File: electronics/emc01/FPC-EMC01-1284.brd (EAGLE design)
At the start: 100 x 86.6 mm, 59 parts, among them J1 CONN-MOLEX-MICROFIT-6PIN, J10 ICSP, J11 CONN-RECT-16PIN-2ROW, J12 CONN-RECT-16PIN-2ROW, J13 CONN-RECT-16PIN-2ROW, J14 CONN-RECT-16PIN-2ROW, J4 MOT-X, J5 MOT-Y, J6 MOT-Z, J7 CONN-RECT-3PINJST_PH_2MM, J8 CONN-RECT-3PINJST_PH_2MM, J9 CONN-RECT-3PINJST_PH_2MM, Q2 2N7002PW, Q4 16Mhz, U1 STEPSTICK, U2 STEPSTICK, U3 STEPSTICK, U4 MIC5205, U5 ATMEGA1284P-AU, U6 FT231XS

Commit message: Cleaned up EMC01 board and finalized for peer review
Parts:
- removed C18: 100uF, rcl:PANASONIC_D
- removed C19, C24: 0.1uF, SparkFun:0603-CAP
- removed C20: 10uF, SparkFun-Capacitors:EIA3216
- removed C22, C23: 47pF, SparkFun-Capacitors:0603-CAP
- removed C34, C36, C42: 100nF, dp_devices:C805
- removed J10: ICSP, FirePick:CONN-RECT-2.54MM-6-PIN-2ROW-SMTH
- removed JP5: (no value), !con-lstb:MA04-1
- removed LED4: Yellow, SparkFun-LED:LED-1206-NO_SILK
- removed Q4: 16Mhz, adafruit:CTS406
- removed R12: 1k, SparkFun:0603-RES
- removed R13, R16: 27, SparkFun-Resistors:0603-RES
- removed R17, R18: 10k, SparkFun:0603-RES
- removed U$22: USB-MINIB-5PIN, SparkFun-Connectors:USB-MINIB
- removed U4: MIC5205, SparkFun:SOT23-5
- removed U5: ATMEGA1284P-AU, Atmel_By_element14_Batch_1-00:QFP80P1200X1200X120-44N
- removed U6: FT231XS, SparkFun-DigitalIC:SSOP20_L
- added C1, C4, C5, C7, C8: 100N, SparkFun-Capacitors:0805
- added C10: 0.1uF, SparkFun-Capacitors:0805
- added C12: 47pF, SparkFun-Capacitors:0805
- added C9: 0.1, SparkFun-Capacitors:0805
- added FID1, FID2, FID3, FID4: FIDUCIAL1X2, SparkFun-Aesthetics:FIDUCIAL-1X2
- added J15: (no value), !con-lstb:MA04-1
- added J16: ICSP, FirePick:CONN-RECT-2.54MM-6-PIN-2ROW-SMTH
- added J2: CONN-MOLEX-MICROFIT-6PIN, FirePick:CONN-MOLEX-MINIFIT-6PIN-2ROW
- added J4A: MOT-X, FirePick:CONN-JST-PH_2.0MM_4PIN-SMT-RA
- added J5A: MOT-Y, FirePick:CONN-JST-PH_2.0MM_4PIN-SMT-RA
- added J6A: MOT-Z, FirePick:CONN-JST-PH_2.0MM_4PIN-SMT-RA
- added J7A, J8A, J9A: (no value), FirePick:CONN-JST_PH-2.0MM-3PIN-SMT-RA
- added LED2: Red, SparkFun-LED:LED-1206-NO_SILK
- added LOGO1: FIREPICK-LOGO, FirePick:FIREPICK-LOGO
- added LOGO2: CC-BY-SA-LOGO, FirePick:CC-BY-SA-LOGO
- added LOGO3: OSHW-LOGOL, SparkFun-Aesthetics:OSHW-LOGO-L
- added R1: 10K, SparkFun-Resistors:0805
- added R6: 1k, SparkFun-Resistors:0805
- added R8: 27, SparkFun-Resistors:0805
- added STEPSTICK1, STEPSTICK2: STEPSTICK, FirePick:STEPSTICK
- added TP1: PD2, FirePick:CON-TESTPOINT
- added TP2: +12V, FirePick:CON-TESTPOINT
- added TP3: GND, FirePick:CON-TESTPOINT
- added TP4: +5V, FirePick:CON-TESTPOINT
- added TP5: +3.3V, FirePick:CON-TESTPOINT
- added U$15: CREATIVE_COMMONS, SparkFun:CREATIVE_COMMONS
- added X1: 16Mhz, adafruit:CTS406
- C11, C3: value 22pF -> 22P; device dp_devices:C805 -> SparkFun-Capacitors:0805
- C13: value 100nF -> 47pF; device dp_devices:C805 -> SparkFun-Capacitors:0805
- C14: value 100nF -> 0.1uF; device dp_devices:C805 -> SparkFun-Capacitors:0805
- C15: value 1uF -> 100uF; device SparkFun:0603-CAP -> rcl:PANASONIC_D
- C17: value 0.1uF -> 100uF; device SparkFun:0603-CAP -> rcl:PANASONIC_D
- C2: value 0.1uF -> 10uF; device ipc-7351-capacitor:CAPC2012X145AN -> rcl:PANASONIC_D
- C6: value 100uF -> 0.1uF; device rcl:PANASONIC_D -> SparkFun-Capacitors:0805
- J1: value CONN-MOLEX-MICROFIT-6PIN -> USB-MINIB-5PIN; device FirePick:CONN-MOLEX-MINIFIT-6PIN-2ROW -> SparkFun-Connectors:USB-MINIB
- J4: value MOT-X -> (none); device FirePick:CONN-JST-PH_2.0MM_4PIN-SMT-RA -> !con-lstb:MA04-1
- J5: value MOT-Y -> (none); device FirePick:CONN-JST-PH_2.0MM_4PIN-SMT-RA -> !con-lstb:MA04-1
- J6: value MOT-Z -> (none); device FirePick:CONN-JST-PH_2.0MM_4PIN-SMT-RA -> !con-lstb:MA04-1
- J7, J8, J9: value CONN-RECT-3PINJST_PH_2MM -> (none); device FirePick:CONN-JST_PH-2.0MM-3PIN-SMT-RA -> !con-lstb:MA03-1
- LED3: value Red -> Yellow
- R10, R11: value 1k -> 10k; device SparkFun:0603-RES -> SparkFun-Resistors:0805
- R2: device adafruit:R0805 -> SparkFun-Resistors:0805
- R3, R4, R5: value 10K -> 1k; device adafruit:R0805 -> SparkFun-Resistors:0805
- R7: device SparkFun:0603-RES -> SparkFun-Resistors:0805
- R9: value 1k -> 27; device SparkFun:0603-RES -> SparkFun-Resistors:0805
- U1: value STEPSTICK -> IC-ATMEGA1284P-AU; device FirePick:STEPSTICK -> FirePick:QFP44
- U2: value STEPSTICK -> FT231XS; device FirePick:STEPSTICK -> SparkFun-DigitalIC:SSOP20_L
- moved J1 73.0 mm to (50.0, 12.0), turned to 90 degrees
- moved C6 63.6 mm to (54.5, 18.6), turned to 270 degrees
- moved C15 46.4 mm to (50.3, 70.6), turned to 180 degrees
- moved C14 42.2 mm to (42.2, 19.5), turned to 90 degrees
- moved R5 40.3 mm to (65.3, 20.4)
- moved C13 39.3 mm to (52.7, 18.6), turned to 90 degrees
- moved R4 35.2 mm to (65.3, 17.5)
- moved C17 32.4 mm to (69.5, 38.9), turned to 60 degrees
- moved J3 31.7 mm to (50.0, 32.0), turned to 180 degrees
- moved Q2 31.2 mm to (59.6, 24.8), turned to 270 degrees
- moved R3 28.1 mm to (65.3, 14.6)
- moved R2 26.2 mm to (55.4, 40.2), turned to 270 degrees
- moved U2 24.2 mm to (50.0, 24.8), turned to 180 degrees
- moved S1 23.6 mm to (62.1, 10.4)
- moved R7 22.7 mm to (50.8, 29.5), turned to 0 degrees
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- renumbered U3 to STEPSTICK3
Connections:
- removed net !XYZ-ENABLE: R2.1, R3.1, R4.1, STEPSTICK3.!ENABLE!, U1.!ENABLE!, U2.!ENABLE!, U5.15
- removed net N$1: J5.4, U2.2B
- removed net N$13: J5.3, U2.2A
- removed net N$14: J5.2, U2.1A
- removed net N$15: J5.1, U2.1B
- removed net N$17: J6.4, STEPSTICK3.2B
- removed net N$18: J6.3, STEPSTICK3.2A
- removed net N$19: J6.2, STEPSTICK3.1A
- removed net N$20: J6.1, STEPSTICK3.1B
- removed net N$26: Q2.2, R17.1, U6.1
- removed net N$6: J4.4, U1.2B
- removed net N$7: J4.3, U1.2A
- removed net N$8: J4.2, U1.1A
- removed net N$9: J4.1, U1.1B
- removed net RESERVED: U5.44
- removed net X-STOP: J7.1, U5.21
- removed net Y-STOP: J8.1, U5.22
- removed net Z-STOP: J9.1, U5.23
- new net !XYZ_ENABLE: R2.1, STEPSTICK1.!ENABLE!, STEPSTICK2.!ENABLE!, STEPSTICK3.!ENABLE!, U1.15
- new net DTR_3.3V: Q2.2, R10.1, U2.1
- new net SPARE: TP1.1, U1.11
- new net X1A: J4.2, J4A.2, STEPSTICK1.1A
- new net X1B: J4.1, J4A.1, STEPSTICK1.1B
- new net X2A: J4.3, J4A.3, STEPSTICK1.2A
- new net X2B: J4.4, J4A.4, STEPSTICK1.2B
- new net X_STOP: J7.1, J7A.1, U1.24
- new net Y1A: J5.2, J5A.2, STEPSTICK2.1A
- new net Y1B: J5.1, J5A.1, STEPSTICK2.1B
- new net Y2A: J5.3, J5A.3, STEPSTICK2.2A
- new net Y2B: J5.4, J5A.4, STEPSTICK2.2B
- new net Y_STOP: J8.1, J8A.1, U1.42
- new net Z1A: J6.2, J6A.2, STEPSTICK3.1A
- new net Z1B: J6.1, J6A.1, STEPSTICK3.1B
- new net Z2A: J6.3, J6A.3, STEPSTICK3.2A
- new net Z2B: J6.4, J6A.4, STEPSTICK3.2B
- new net Z_STOP: J9.1, J9A.1, U1.12
- net !RESET: now also C9.2, J16.2, R1.1, U1.4; no longer C2.1, J10.2, R5.1, U5.4
- net +5V: now also C1.1, C2.+, C5.1, C6.1, C7.1, C8.1, J15.1, J16.5, J7A.2, J8A.2, J9A.2, R1.2, R11.2, R4.1, R5.1, STEPSTICK1.MS1, STEPSTICK1.MS2, STEPSTICK1.MS3, STEPSTICK1.VDD, STEPSTICK2.MS1, STEPSTICK2.MS2, STEPSTICK2.MS3, STEPSTICK2.VDD, TP4.1, U1.17, U1.27, U1.38, U1.5, U2.15; no longer C13.2, C14.2, C19.1, C20.A, C34.2, C36.2, J10.5, JP5.1, R10.1, R18.2, R4.2, R5.2, R7.2, R9.1, U1.MS1, U1.MS2, U1.MS3, U1.VDD, U2.MS1, U2.MS2, U2.MS3, U2.VDD, U4.1, U4.3, U5.17, U5.27, U5.38, U5.5, U6.15
- net 12V: now also C15.+, C17.+, J2.1, J2.2, J2.3, STEPSTICK1.VMOT, STEPSTICK2.VMOT, TP2.1; no longer C18.+, C6.+, J1.1, J1.2, J1.3, U1.VMOT, U2.VMOT
- net 3.3V: now also C10.1, R10.2, TP5.1, U2.13, U2.14, U2.3; no longer C15.1, C24.1, R17.2, U4.5, U6.13, U6.14, U6.3
- net AREF: now also C4.1, U1.29; no longer C42.2, U5.29
- net AVR_RXD: now also R6.1, U1.9; no longer R11.1, U5.9
- net AVR_TXD: now also R7.1, U1.10; no longer R12.1, U5.10
- net D+: now also C13.1, J1.D+, R9.1; no longer C22.1, R16.1, U$22.D+
- net D-: now also C12.1, J1.D-, R8.1; no longer C23.1, R13.1, U$22.D-
- net DTR: now also C9.1, R11.1; no longer C2.2, R18.1
- net GND: now also C1.2, C10.2, C12.2, C13.2, C14.2, C15.-, C17.-, C2.-, C4.2, C5.2, C6.2, C7.2, C8.2, J1.GND, J1.MTN1, J1.MTN2, J1.MTN3, J1.MTN4, J15.2, J16.1, J2.4, J2.5, J2.6, J7A.3, J8A.3, J9A.3, STEPSTICK1.GND, STEPSTICK1.GND@2, STEPSTICK2.GND, STEPSTICK2.GND@2, TP3.1, U1.18, U1.28, U1.39, U1.6, U2.16, U2.6; no longer C13.1, C14.1, C15.2, C17.2, C18.-, C19.2, C20.C, C22.2, C23.2, C24.2, C34.1, C36.1, C42.1, C6.-, J1.4, J1.5, J1.6, J10.1, JP5.2, U$22.GND, U$22.MTN1, U$22.MTN2, U$22.MTN3, U$22.MTN4, U1.GND, U1.GND@2, U2.GND, U2.GND@2, U4.2, U5.18, U5.28, U5.39, U5.6, U6.16, U6.6
- net MISO: now also J16.6, U1.2; no longer J10.6, U5.2
- net MOSI: now also J16.3, U1.1; no longer J10.3, U5.1
- net N$11: now also STEPSTICK1.!RESET!, STEPSTICK1.!SLEEP!; no longer U1.!RESET!, U1.!SLEEP!
- net N$16: now also STEPSTICK2.!RESET!, STEPSTICK2.!SLEEP!; no longer U2.!RESET!, U2.!SLEEP!
- net N$21: now also LED2.A, R4.2; no longer LED3.A, R9.2
- net N$22: now also LED3.A, R5.2; no longer LED4.A, R10.2
- net N$23: now also R8.2, U2.12; no longer R13.2, U6.12
- net N$25: now also R9.2, U2.11; no longer R16.2, U6.11
- net N$4: now also R3.1; no longer R7.1
- net RXD: now also R7.2, U2.4; no longer R12.2, U6.4
- net RXLED: now also LED3.C, U2.17; no longer LED4.C, U6.17
- net SCL: now also J15.3, U1.19; no longer JP5.3, U5.19
- net SCLK: now also J16.4, U1.3; no longer J10.4, U5.3
- net SDA: now also J15.4, U1.20; no longer JP5.4, U5.20
- net TOOL1_AIN: now also U1.37; no longer U5.37
- net TOOL1_DOUT: now also U1.36; no longer U5.33
- net TOOL1_ENABLE: now also U1.41; no longer U5.14
- net TOOL2_AIN: now also U1.35; no longer U5.36
- net TOOL2_DOUT: now also U1.34; no longer U5.32
- net TOOL2_ENABLE: now also U1.40; no longer U5.13
- net TOOL3_AIN: now also U1.32; no longer U5.35
- net TOOL3_DOUT: now also U1.33; no longer U5.31
- net TOOL3_ENABLE: now also U1.22; no longer U5.12
- net TOOL4_AIN: now also U1.30; no longer U5.34
- net TOOL4_DOUT: now also U1.31; no longer U5.30
- net TOOL4_ENABLE: now also U1.21; no longer U5.11
- net TOOL_DIR: now also U1.16; no longer U5.40
- net TOOL_STEP: now also U1.23; no longer U5.41
- net TXD: now also R6.2, U2.20; no longer R11.2, U6.20
- net TXLED: now also LED2.C, U2.10; no longer LED3.C, U6.10
- net VUSB: now also C14.1, J1.VBUS; no longer C17.1, U$22.VBUS
- net XTAL1: now also U1.8, X1.3; no longer Q4.3, U5.8
- net XTAL2: now also U1.7, X1.1; no longer Q4.1, U5.7
- net X_DIR: now also STEPSTICK1.DIR, U1.25; no longer U1.STEP, U5.24
- net X_STEP: now also STEPSTICK1.STEP, U1.26; no longer U1.DIR, U5.16
- net Y_DIR: now also STEPSTICK2.DIR, U1.43; no longer U2.STEP, U5.26
- net Y_STEP: now also STEPSTICK2.STEP, U1.44; no longer U2.DIR, U5.25
- net Z_DIR: now also STEPSTICK3.DIR, U1.13; no longer STEPSTICK3.STEP, U5.42
- net Z_STEP: now also STEPSTICK3.STEP, U1.14; no longer STEPSTICK3.DIR, U5.43
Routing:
- net GND: track 280.2 -> 167.5 mm, vias 8 -> 24
- net TOOL4_AIN: track 125.6 -> 29.6 mm
- net Y_DIR: track 103.5 -> 14.3 mm, vias 4 -> 1
- net !XYZ-ENABLE: track 84.2 -> 0.00 mm, vias 3 -> 0
- net TOOL2_ENABLE: track 101.5 -> 32.7 mm, vias 3 -> 2
- net !XYZ_ENABLE: track 0.00 -> 67.0 mm, vias 0 -> 3
- net 12V: track 180.7 -> 239.0 mm, vias 20 -> 16
- net MISO: track 76.4 -> 18.9 mm, vias 2 -> 0
- net DTR: track 67.0 -> 13.2 mm, vias 1 -> 0
- net SCLK: track 73.6 -> 22.2 mm, vias 2 -> 1
- net TOOL4_ENABLE: track 84.0 -> 33.8 mm, vias 2 -> 0
- net X_STOP: track 0.00 -> 49.4 mm, vias 0 -> 3
- net X-STOP: track 49.2 -> 0.00 mm, vias 2 -> 0
- net Y-STOP: track 45.9 -> 0.00 mm, vias 2 -> 0
- net Y_STOP: track 0.00 -> 45.8 mm, vias 0 -> 1
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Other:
- board text added: "+"
- board text added: "+12V"
- board text added: "+12V PWR IN"
- board text added: "+3.3V"
- board text added: "+5V"
- board text added: "+5V PWR"
- board text added: "/RESET"
- board text added: "ATMEGA1284"
- board text added: "DTR"
- board text added: "FT231X"
- board text added: "GND"
- board text added: "I2C"
- board text added: "ICSP"
- board text added: "MISO"
- board text added: "MODULAR TOOL #1"
- board text added: "MODULAR TOOL #2"
- board text added: "MODULAR TOOL #3"
- board text added: "MODULAR TOOL #4"
- board text added: "MOSI"
- board text added: "P/N: EMC01"
- board text added: "RESET"
- board text added: "RXD"
- board text added: "Released under the Creative Commons Attribution Share-Alike 4.0 License (http://goo.gl/B0gjwG) Design by: Neil Jansen, Sept. 2014"
- board text added: "SCL"
- board text added: "SCLK"
- board text added: "SDA"
- board text added: "SERIAL RX"
- board text added: "SERIAL TX"
- board text added: "SIG"
- board text added: "SPI"
- board text added: "TXD"
- board text added: "USB TO RasPi"
- board text added: "X AXIS"
- board text added: "X ENDSTOP"
- board text added: "X MOT"
- board text added: "Y AXIS"
- board text added: "Y ENDSTOP"
- board text added: "Y MOT"
- board text added: "Z AXIS"
- board text added: "Z ENDSTOP"
- board text added: "Z MOT"

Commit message: Cleanups after peer review
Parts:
- removed LOGO1: FIREPICK-LOGO, FirePick:FIREPICK-LOGO
- removed LOGO2: CC-BY-SA-LOGO, FirePick:CC-BY-SA-LOGO
- removed LOGO3: OSHW-LOGOL, SparkFun-Aesthetics:OSHW-LOGO-L
- added LOGO4: LOGO-FIREPICK, FirePick:LOGO-FIREPICK
- added LOGO5: LOGO-OSHWMEDIUM, FirePick:LOGO-OSHW-MEDIUM
- added LOGO6: LOGO-CC-BY-SA, FirePick:LOGO-CC-BY-SA
- C2: value 10uF -> 4.7uF
- J15, J3: value (none) -> DNP
- moved R3 5.10 mm to (60.2, 14.6), turned to 180 degrees
- moved R4 5.10 mm to (60.2, 17.5), turned to 0 degrees
- moved R5 5.00 mm to (60.3, 20.4), turned to 0 degrees
- moved LED1 3.20 mm to (64.4, 14.6), turned to 0 degrees
- moved LED2 3.20 mm to (64.4, 17.5), turned to 0 degrees
- moved LED3 3.10 mm to (64.3, 20.4), turned to 0 degrees
- moved J4 0.90 mm to (36.9, 90.0)
- moved J4A 0.90 mm to (36.9, 88.0)
- moved J2 0.50 mm to (50.5, 85.0)
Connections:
- net +5V: no longer J11.14, J12.14, J13.14, J14.14
- net GND: now also J11.14, J12.14, J13.14, J14.14; no longer J12.7, J13.8, J14.7, J14.8
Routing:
- net N$2: track 20.9 -> 2.61 mm
- net +5V: track 105.8 -> 88.9 mm
- net RXLED: track 12.2 -> 20.3 mm
- net 12V: track 239.0 -> 245.2 mm, vias 16 -> 0
- net N$3: track 5.92 -> 0.00 mm
- net GND: track 167.5 -> 172.8 mm
- net N$24: track 2.54 -> 5.97 mm
- net N$16: track 2.54 -> 5.63 mm
- net !RESET: track 129.0 -> 125.9 mm
- net TXLED: track 24.7 -> 27.7 mm
- net N$11: track 2.54 -> 5.09 mm
- net 3.3V: track 43.0 -> 45.0 mm
- net X1B: track 30.1 -> 29.1 mm
- net X2A: track 30.0 -> 29.1 mm
- net X2B: track 29.5 -> 28.6 mm
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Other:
- board text added: "1284"
- board text added: "ATMEGA"
- board text added: "RST"
- board text added: "http://delta.firepick.org"
- board text removed: "ATMEGA1284"
- board text removed: "RESET"

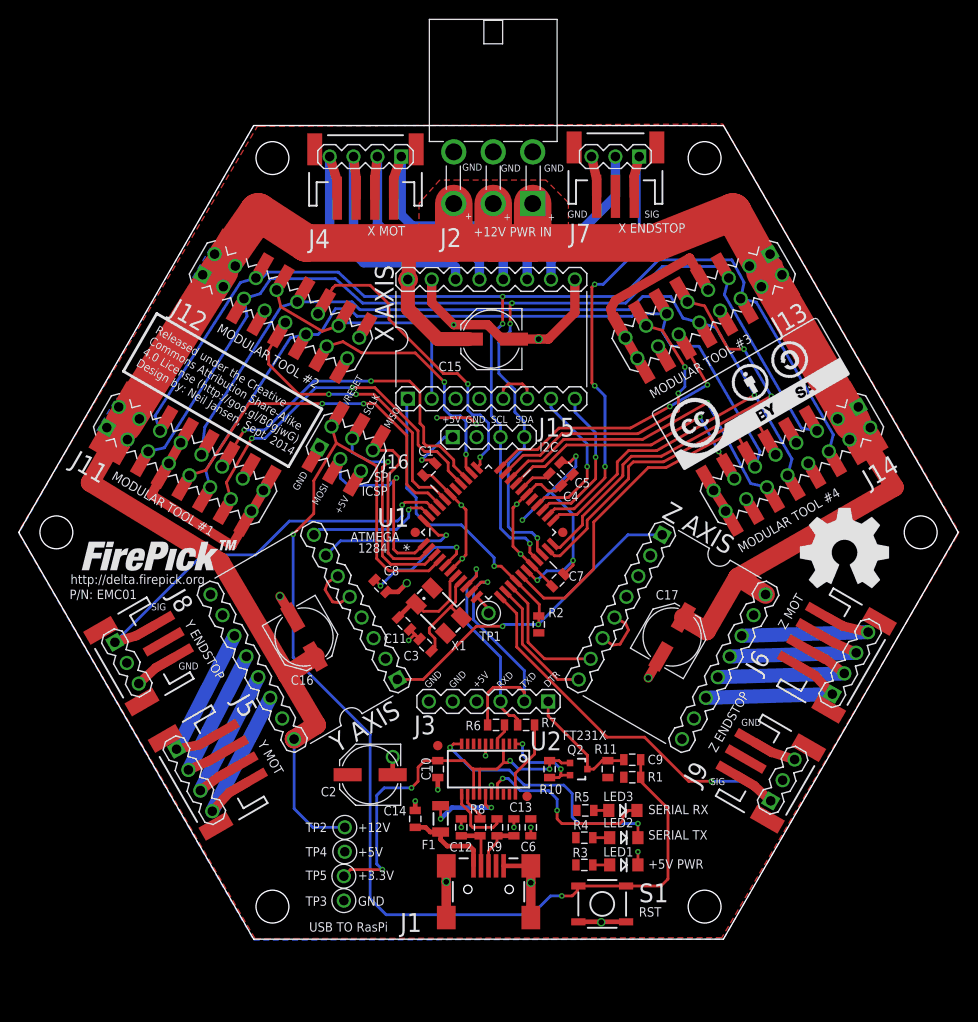
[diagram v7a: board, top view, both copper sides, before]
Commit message: Fixed minor issues and changed modular tool connector pinout to allow better routing of GND and +12V planes
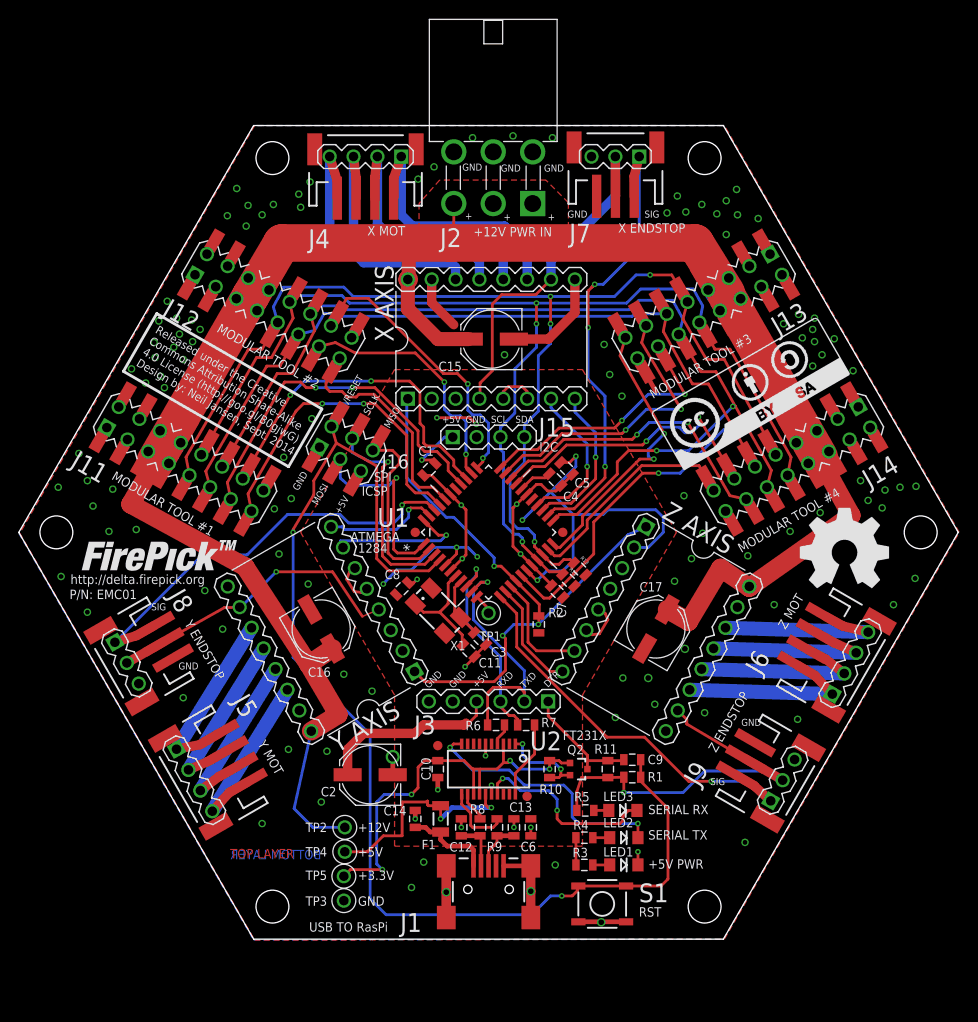
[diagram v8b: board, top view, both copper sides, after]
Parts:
- removed U$15: CREATIVE_COMMONS, SparkFun:CREATIVE_COMMONS
- added R12, R13: 10K, SparkFun-Resistors:0805
- moved C11 7.48 mm to (47.9, 37.4)
- moved C3 5.84 mm to (49.1, 38.7), turned to 315 degrees
- moved C8 2.32 mm to (40.8, 44.0), turned to 45 degrees
- moved C16 2.01 mm to (32.2, 39.7)
- moved STEPSTICK2 2.01 mm to (32.2, 39.7)
- moved C17 1.92 mm to (67.8, 39.7)
- moved STEPSTICK3 1.92 mm to (67.8, 39.7)
- moved C7 1.20 mm to (57.3, 43.7), turned to 135 degrees
- moved J12 0.81 mm to (27.1, 74.1)
- moved X1 0.10 mm to (44.6, 41.7)
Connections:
- net +5V: now also R12.2, R13.2, STEPSTICK3.VDD
- net 12V: now also J11.5, J11.6, J11.7, J11.8, J12.5, J12.6, J12.7, J12.8, J13.5, J13.6, J13.7, J13.8, J14.5, J14.6, J14.7, J14.8; no longer J11.1, J11.2, J11.3, J11.4, J12.1, J12.2, J12.3, J12.4, J13.1, J13.2, J13.3, J13.4, J14.1, J14.2, J14.3, J14.4
- net GND: now also J11.1, J11.2, J11.3, J12.1, J12.2, J12.3, J12.4, J13.1, J13.2, J13.3, J13.4, J14.1, J14.2, J14.3; no longer J11.14, J11.15, J11.7, J11.8, J12.14, J12.15, J12.16, J12.8, J13.14, J13.15, J13.7, J14.14, J14.15, J14.16
- net SCL: now also J11.10, J12.10, J13.10, J14.10, R12.1; no longer J11.6, J12.6, J13.6, J14.6
- net SDA: now also J11.9, J12.9, J13.9, J14.9, R13.1; no longer J11.5, J12.5, J13.5, J14.5
- net TOOL1_DOUT: now also J11.14; no longer J11.12
- net TOOL1_ENABLE: now also J11.15; no longer J11.9
- net TOOL2_DOUT: now also J12.14; no longer J12.12
- net TOOL2_ENABLE: now also J12.15; no longer J12.9
- net TOOL3_DOUT: now also J13.14; no longer J13.12
- net TOOL3_ENABLE: now also J13.15; no longer J13.9
- net TOOL4_DOUT: now also J14.14; no longer J14.12
- net TOOL4_ENABLE: now also J14.15; no longer J14.9
- net TOOL_STEP: now also J11.12, J12.12, J13.12, J14.12; no longer J11.10, J12.10, J13.10, J14.10
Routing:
- net +5V: track 88.9 -> 220.3 mm, vias 9 -> 11
- net GND: track 172.8 -> 91.0 mm, vias 24 -> 124
- net 12V: track 245.2 -> 216.2 mm
- net TOOL3_ENABLE: track 44.8 -> 30.7 mm
- net TOOL4_ENABLE: track 33.8 -> 23.9 mm
- net TOOL2_ENABLE: track 32.7 -> 24.3 mm, vias 2 -> 0
- net TOOL_DIR: track 121.6 -> 113.7 mm, vias 0 -> 2
- net SCL: track 129.7 -> 122.3 mm
- net XTAL1: track 11.0 -> 6.61 mm
- net TOOL4_DOUT: track 35.2 -> 32.1 mm, vias 1 -> 2
- net TOOL2_DOUT: track 33.8 -> 30.8 mm
- net TOOL_STEP: track 111.8 -> 108.9 mm, vias 1 -> 2
- net TOOL1_ENABLE: track 38.1 -> 35.2 mm
- net N$2: track 2.61 -> 0.00 mm
- net TOOL3_DOUT: track 31.2 -> 28.7 mm
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- added copper zone on layer 1, net GND
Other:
- board text added: "BOTTOM LAYER"
- board text added: "TOP LAYER"
